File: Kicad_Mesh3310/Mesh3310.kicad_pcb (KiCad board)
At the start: 4 copper layers, 41.4 x 108 mm, 211 parts, among them J10 Speaker pad, J11 GNSS antenne (U.FL), J2 Mic pad, J3 Sim/Pad, J4 Conn_01x05_Pin, J5 Vibrator pad, J6 Buzzer pad, J7 Display, J8 LTE antenne: U.FL -> flexante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, J9 Battery, Q1 BC847, Q4 BSS138, Q5 BSS138, Q6 IRLML6401, Q7 BSS138, SW18 POWER ON/OFF, SW2 "OK", U1 TPE4259-63, U10 SX1262IMLTRT, U12 nRF9151-LAXX, U13 NRF52840-QIAA-R, U14 TPS63031DSK, U2 MX25R1635FZUIH0, U3 BQ24074RGT, U4 MX25R1635FZNIH0, U5 MAX98357A, U6 SIM-ST-MFF2, U7 USBLC6-2P6, U8 SKY65723-81, U9 MAX16054, X1 S201632M10PF10PPM 32MHz, X2 S201632M10PF10PPM 32MHz, X4 32.768KHz

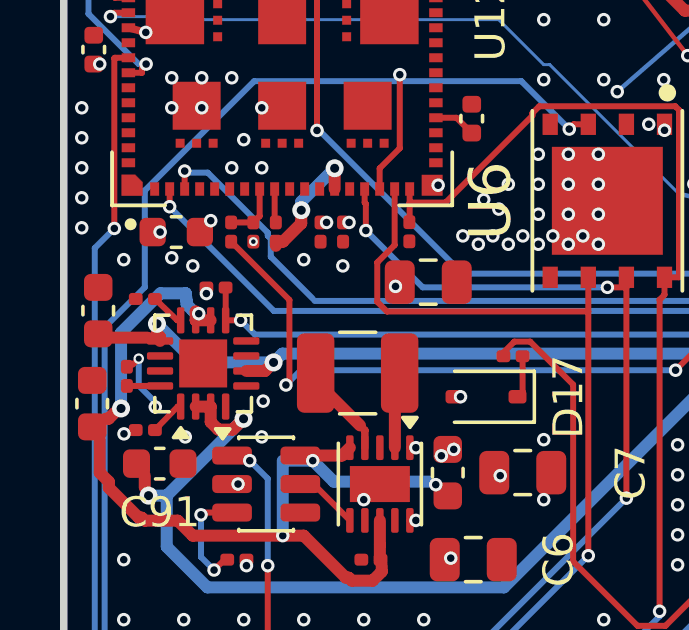
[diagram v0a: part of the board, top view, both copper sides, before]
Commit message: Rev. C: schemafixes uit datasheetcontrole (VDD-buffer nRF9151, DC-blok LoRa, DNP C70/C71/BT2, deler 1M, laadtimers aan)
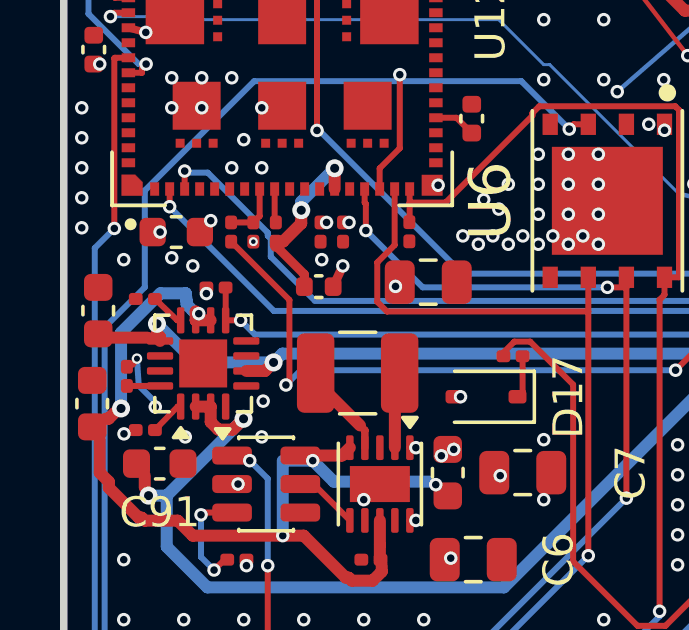
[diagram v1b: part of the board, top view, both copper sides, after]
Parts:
- added C95: 10u, Capacitor_SMD:C_0402_1005Metric, F.Cu at (128.5, 78.9)
- C96: renamed from R6; value 0R -> 56pF; footprint Resistor_SMD:R_0201_0603Metric -> Capacitor_SMD:C_0201_0603Metric
- R59, R60: value 47k -> 1M
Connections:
- U3 pad 14: GND -> unconnected-(U3-TMR-Pad14)
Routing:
- net Net-(U12-VDD): track 6.87 -> 8.62 mm
- net GND: track 33.3 -> 34.1 mm
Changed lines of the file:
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@@
 	(net 222 "/P0.08_DSP_SCK")
 	(net 223 "Net-(J8-In)")
+	(net 224 "unconnected-(U3-TMR-Pad14)")
 	(footprint "Resistor_SMD:R_0201_0603Metric"
 		(layer "F.Cu")
@@
 		(sheetname "/POWER/")
 		(sheetfile "power.kicad_sch")
-		(attr smd)
+		(attr smd exclude_from_bom dnp)
 		(fp_line
 			(start -1.61 0.85)
@@
 			)
 		)
-		(property "Value" "47k"
+		(property "Value" "1M"
 			(at 0 1.05 90)
 			(layer "F.Fab")
@@
 		(sheetname "/LORA/")
 		(sheetfile "rf.kicad_sch")
-		(attr smd)
+		(attr smd exclude_from_bom dnp)
 		(fp_rect
 			(start -0.7 -0.35)
@@
 			)
 		)
-		(property "Value" "47k"
+		(property "Value" "1M"
 			(at 0 1.05 90)
 			(layer "F.Fab")
@@
 		(sheetname "/POWER/")
 		(sheetfile "power.kicad_sch")
-		(attr smd)
+		(attr smd exclude_from_bom dnp)
 		(fp_poly
 			(pts
@@
 		)
 	)
-	(footprint "Resistor_SMD:R_0201_0603Metric"
+	(footprint "Capacitor_SMD:C_0201_0603Metric"
 		(layer "F.Cu")
 		(at 137.47 55.21 180)
-		(descr "Resistor SMD 0201 (0603 Metric), square (rectangular) end terminal, IPC-7351 nominal, (Body size source: https://www.vishay.com/docs/20052/crcw0201e3.pdf), generated with kicad-footprint-generator")
-		(tags "resistor")
-		(property "Reference" "R6"
+		(descr "Capacitor SMD 0201 (0603 Metric), square (rectangular) end terminal, IPC-7351 nominal, (Body size source: https://www.vishay.com/docs/20052/crcw0201e3.pdf), generated with kicad-footprint-generator")
+		(tags "capacitor")
+		(property "Reference" "C96"
 			(at 0 -1.05 180)
 			(layer "F.SilkS")
@@
 			)
 		)
-		(property "Value" "0R"
+		(property "Value" "56pF"
 			(at 0 1.05 180)
 			(layer "F.Fab")
@@
 			)
 		)
-		(property "Datasheet" "https://jlcpcb.com/partdetail/25819-0402WGF1000TCE/C25076"
+		(property "Datasheet" ""
 			(at 0 0 180)
 			(layer "F.Fab")
@@
 			)
 		)
-		(property "Description" "Resistor, small symbol"
+		(property "Description" "Unpolarized capacitor, small symbol"
 			(at 0 0 180)
 			(layer "F.Fab")
@@
 			)
 		)
-		(property "LCSC" "C25076"
+		(property "LCSC" "C2183491"
 			(at 0 0 180)
 			(unlocked yes)
@@
 		)
 		(embedded_fonts no)
-		(model "${KICAD9_3DMODEL_DIR}/Resistor_SMD.3dshapes/R_0201_0603Metric.step"
+		(model "${KICAD9_3DMODEL_DIR}/Capacitor_SMD.3dshapes/C_0201_0603Metric.step"
 			(offset
 				(xyz 0 0 0)
@@
 		(sheetname "/POWER/")
 		(sheetfile "power.kicad_sch")
-		(attr smd exclude_from_bom)
+		(attr smd exclude_from_bom dnp)
 		(fp_poly
 			(pts
@@
 		(sheetname "/LORA/")
 		(sheetfile "rf.kicad_sch")
-		(attr smd)
+		(attr smd exclude_from_bom dnp)
 		(fp_rect
 			(start -0.7 -0.35)
@@
 			(layers "F.Cu" "F.Mask" "F.Paste")
 			(roundrect_rratio 0.25)
-			(net 13 "GND")
+			(net 224 "unconnected-(U3-TMR-Pad14)")
 			(pinfunction "TMR")
-			(pintype "input")
+			(pintype "input+no_connect")
 		)
 		(pad "15" smd roundrect
@@
 		)
 	)
+	(footprint "Capacitor_SMD:C_0402_1005Metric"
+		(layer "F.Cu")
+		(at 128.5 78.9)
+		(descr "Capacitor SMD 0402 (1005 Metric), square (rectangular) end terminal, IPC-7351 nominal, (Body size source: IPC-SM-782 page 76, https://www.pcb-3d.com/wordpress/wp-content/uploads/ipc-sm-782a_amendment_1_and_2.pdf), generated with kicad-footprint-generator")
+		(tags "capacitor")
+		(property "Reference" "C95"
+			(at 0 -1.16)
+			(layer "F.SilkS")
+			(hide yes)
+			(effects
+				(font
+					(size 1 1)
+					(thickness 0.15)
+				)
+			)
+		)
+		(property "Value" "10u"
+			(at 0 1.16)
+			(layer "F.Fab")
+			(effects
+				(font
+					(size 1 1)
+					(thickness 0.15)
+				)
+			)
+		)
+		(property "Datasheet" ""
+			(at 0 0)
+			(layer "F.Fab")
+			(hide yes)
+			(effects
+				(font
+					(size 1.27 1.27)
+					(thickness 0.15)
+				)
+			)
+		)
+		(property "Description" ""
+			(at 0 0)
+			(layer "F.Fab")
+			(hide yes)
+			(effects
+				(font
+					(size 1.27 1.27)
+					(thickness 0.15)
+				)
+			)
+		)
+		(attr smd)
+		(fp_line
+			(start -0.107836 -0.36)
+			(end 0.107836 -0.36)
+			(stroke
+				(width 0.12)
+				(type solid)
+			)
+			(layer "F.SilkS")
+		)
+		(fp_line
+			(start -0.107836 0.36)
+			(end 0.107836 0.36)
+			(stroke
+				(width 0.12)
+				(type solid)
+			)
+			(layer "F.SilkS")
+		)
+		(fp_rect
+			(start -0.91 -0.46)
+			(end 0.91 0.46)
+			(stroke
+				(width 0.05)
+				(type solid)
+			)
+			(fill no)
+			(layer "F.CrtYd")
+		)
+		(fp_rect
+			(start -0.5 -0.25)
+			(end 0.5 0.25)
+			(stroke
+				(width 0.1)
+				(type solid)
+			)
+			(fill no)
+			(layer "F.Fab")
+		)
+		(fp_text user "${REFERENCE}"
+			(at 0 0)
+			(layer "F.Fab")
+			(effects
+				(font
+					(size 0.25 0.25)
+					(thickness 0.04)
+				)
+			)
+		)
+		(pad "1" smd roundrect
+			(at -0.48 0)
+			(size 0.56 0.62)
+			(layers "F.Cu" "F.Mask" "F.Paste")
+			(roundrect_rratio 0.25)
+			(net 113 "Net-(U12-VDD)")
+		)
+		(pad "2" smd roundrect
+			(at 0.48 0)
+			(size 0.56 0.62)
+			(layers "F.Cu" "F.Mask" "F.Paste")
+			(roundrect_rratio 0.25)
+			(net 13 "GND")
+		)
+		(embedded_fonts no)
+		(model "${KICAD9_3DMODEL_DIR}/Capacitor_SMD.3dshapes/C_0402_1005Metric.step"
+			(offset
+				(xyz 0 0 0)
+			)
+			(scale
+				(xyz 1 1 1)
+			)
+			(rotate
+				(xyz 0 0 0)
+			)
+		)
+	)
 	(footprint "Resistor_SMD:R_0201_0603Metric"
 		(layer "F.Cu")
@@
 	)
 	(segment
-		(start 122.5 81.3)
+		(start 122.44 81.3)
 		(end 122.3 81.5)
 		(width 0.2)
@@
 	)
 	(via
-		(at 128 78)
+		(at 128.6 78)
 		(size 0.45)
 		(drill 0.25)
@@
 	)
 	(via
-		(at 122.5 81.3)
+		(at 122.44 81.3)
 		(size 0.35)
 		(drill 0.2)
@@
 	(segment
 		(start 122.5 82.2)
-		(end 122.5 81.3)
+		(end 122.44 81.3)
 		(width 0.2)
 		(layer "B.Cu")
@@
 		(net 81)
 	)
+	(segment
+		(start 127.07 77.54)
+		(end 128.02 78.49)
+		(width 0.3)
+		(layer "F.Cu")
+		(net 113)
+	)
+	(segment
+		(start 128.02 78.49)
+		(end 128.02 78.9)
+		(width 0.3)
+		(layer "F.Cu")
+		(net 113)
+	)
+	(segment
+		(start 128.98 78.9)
+		(end 129.302 78.209)
+		(width 0.3)
+		(layer "F.Cu")
+		(net 13)
+	)
 	(zone
